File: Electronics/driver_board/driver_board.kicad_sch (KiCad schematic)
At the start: 0 parts

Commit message: [pcb] Added MCU, current sense parts
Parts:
- added J1: Conn_ST_STDC14, Connector_PinHeader_1.27mm:PinHeader_2x07_P1.27mm_Vertical_SMD, symbol Connector:Conn_ST_STDC14
- added R1: 7m, Resistor_SMD:R_2512_6332Metric, symbol Device:R_Small
- added U1: INA241A2xDDF, Package_TO_SOT_SMD:SOT-23-8, symbol Amplifier_Current:INA241A2xDDF
- added U2: STM32G491CCT6, Package_QFP:LQFP-48_7x7mm_P0.5mm, symbol DWlib:STM32G491CCT6
- added U3: REF3433TIDBVR, Package_TO_SOT_SMD:SOT-23-6, symbol DWlib:REF3433TIDBVR
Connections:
- new net: U1.2 (GND), U1.4 (GND)
- new net: J1.5 (GND), J1.7 (GND)
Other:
- company: (none) -> D. Watman

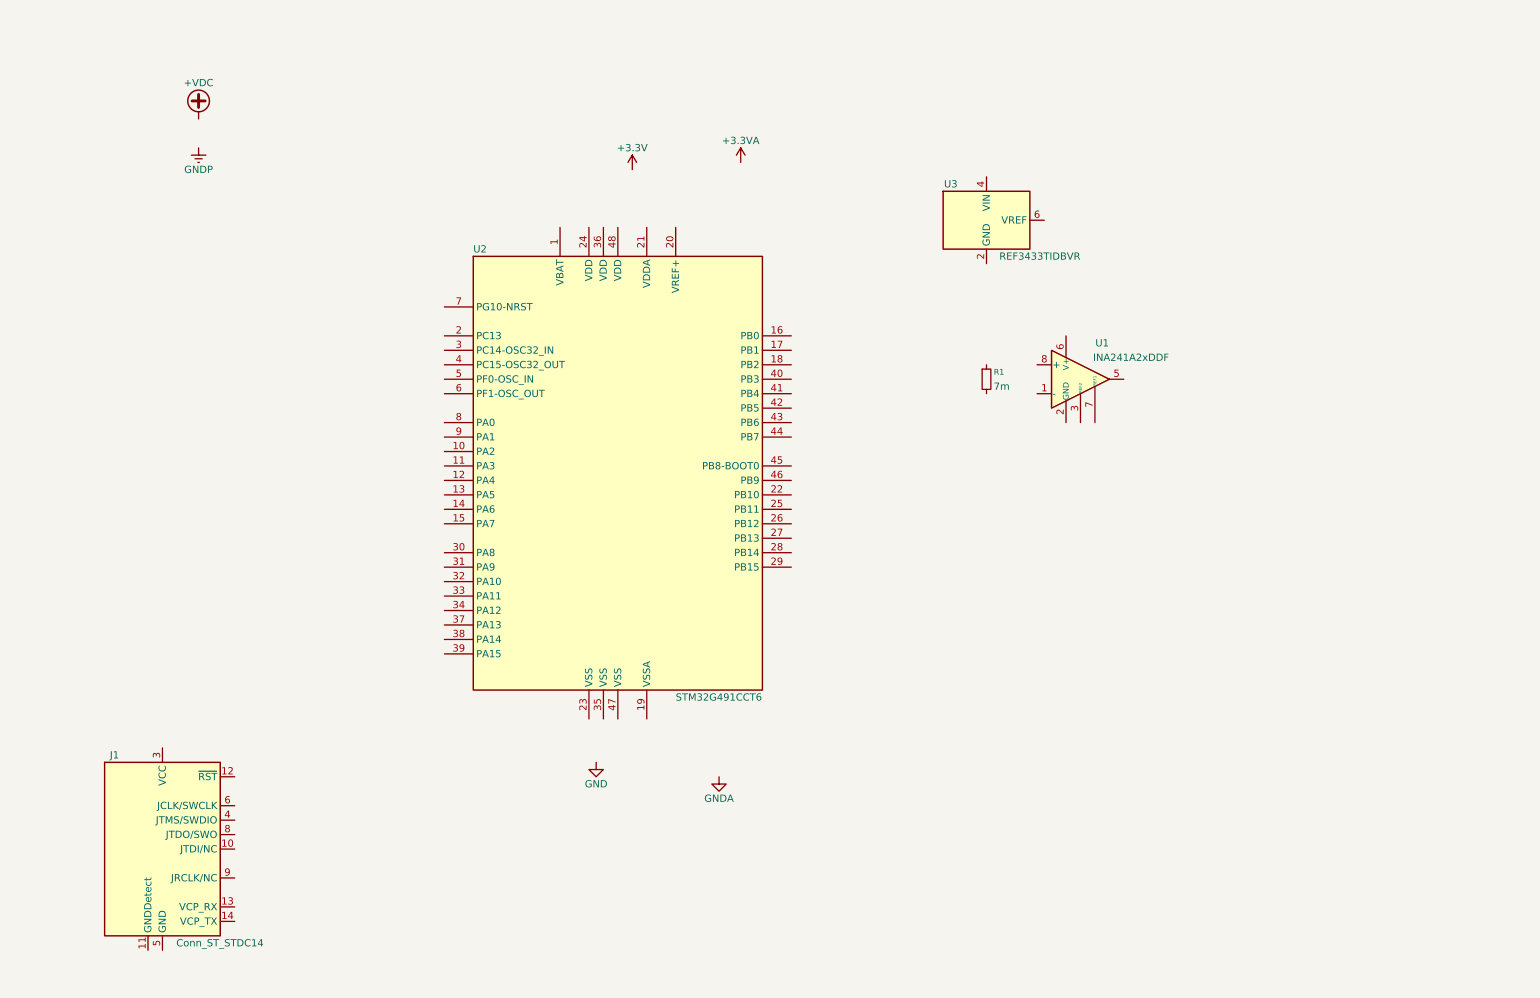
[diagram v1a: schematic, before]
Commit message: Added H-bridge
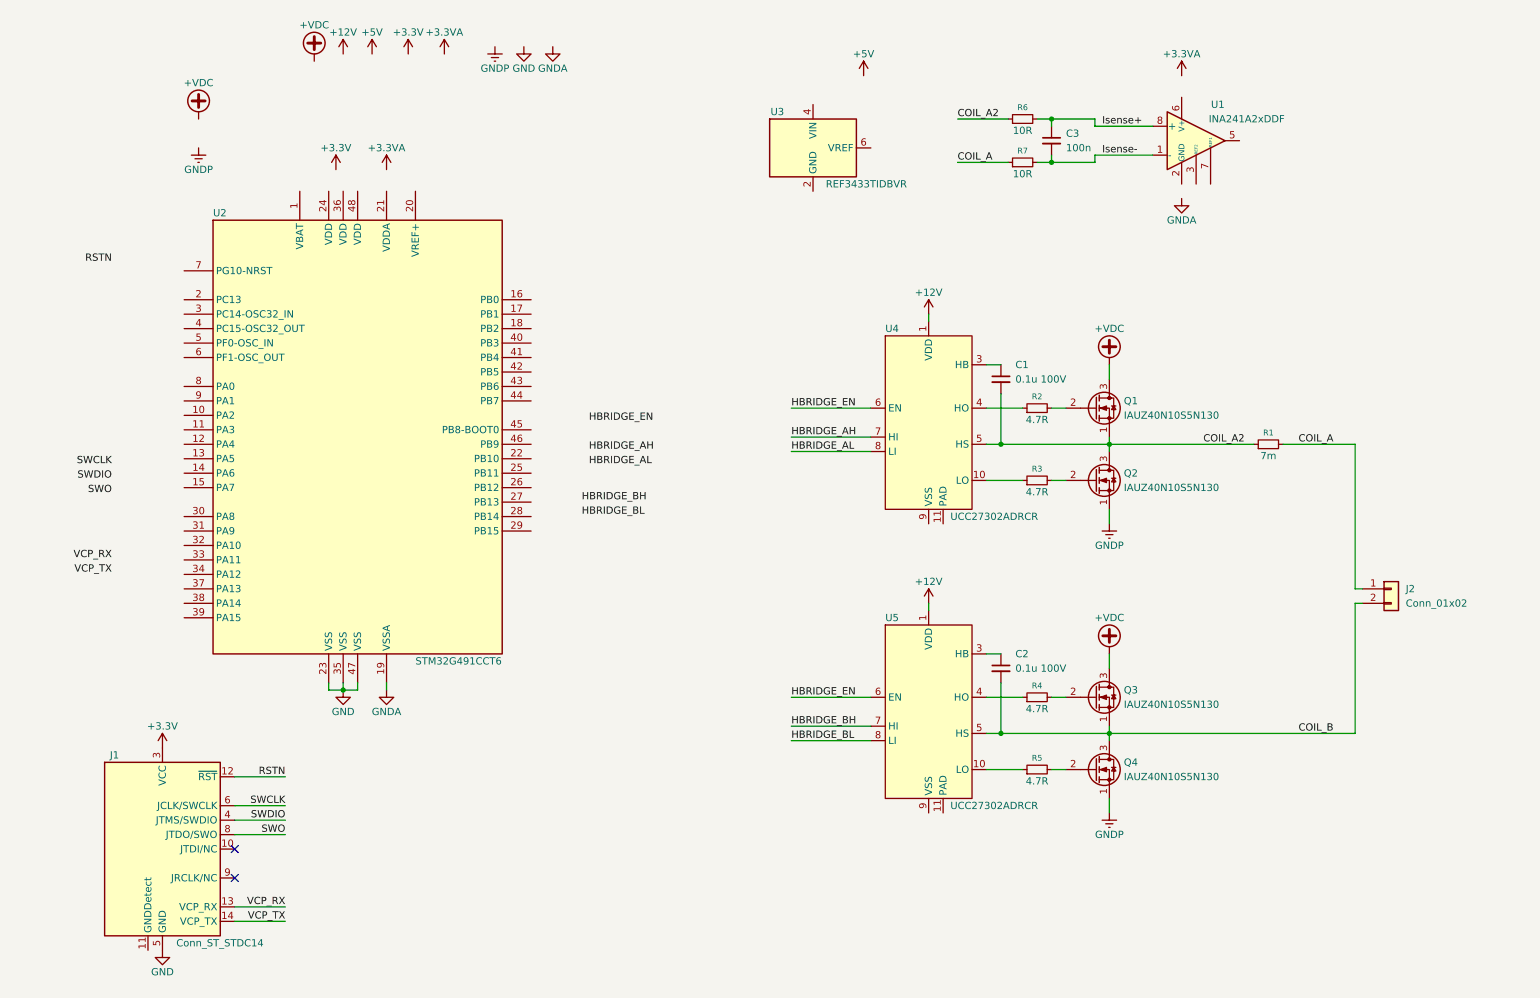
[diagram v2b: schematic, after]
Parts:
- added C1, C2: 0.1u 100V, symbol Device:C_Small
- added C3: 100n, symbol Device:C_Small
- added J2: Conn_01x02, symbol Connector_Generic:Conn_01x02
- added Q1, Q2, Q3, Q4: IAUZ40N10S5N130, DWlib:Infineon_PG-TSDSON-8-33, symbol DWlib:IAUZ40N10S5N130
- added R2, R3, R4, R5: 4.7R, symbol Device:R_Small
- added R6, R7: 10R, symbol Device:R_Small
- added U4, U5: UCC27302ADRCR, DWlib:TI_VSON-10-1EP_3x3mm_P0.5mm_EP1.65x2.4mm, symbol DWlib:UCC27302ADRCR
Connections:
- net +3.3V: now also J1.3 (VCC)
- net +VDC: now also Q1.3 (D), Q3.3 (D)
- net GND: now also J1.5 (GND), J1.7 (GND), U2.23 (VSS), U2.35 (VSS), U2.47 (VSS)
- net GNDA: now also U2.19 (VSSA)
- net GNDP: now also Q2.1 (S), Q4.1 (S)
- net COIL_A2: now reaches R1.1
- net COIL_A2: now also C1.2, Q1.1 (S), Q2.3 (D), R6.1, U4.5 (HS)
- net COIL_A: now reaches R1.2
- net COIL_A: now also J2.1 (Pin_1), R7.1
- net Isense-: now reaches U1.1 (-)
- net Isense-: now also C3.2, R7.2
- net Isense+: now reaches U1.8 (+)
- net Isense+: now also C3.1, R6.2
- net RSTN: now reaches J1.12 (~{RST})
- net VCP_RX: now reaches J1.13 (VCP_RX)
- net VCP_TX: now reaches J1.14 (VCP_TX)
- net SWDIO: now reaches J1.4 (JTMS/SWDIO)
- net SWCLK: now reaches J1.6 (JCLK/SWCLK)
- net SWO: now reaches J1.8 (JTDO/SWO)
- new net: C1.1, U4.3 (HB)
- new net: Q4.2 (G), R5.2
- new net: Q2.2 (G), R3.2
- new net: R4.1, U5.4 (HO)
- new net: Q3.2 (G), R4.2
- new net: R3.1, U4.10 (LO)
- new net: R2.1, U4.4 (HO)
- new net: C2.1, U5.3 (HB)
- new net: Q1.2 (G), R2.2
- new net: R5.1, U5.10 (LO)
- new net +12V: U4.1 (VDD), U5.1 (VDD)
- new net COIL_B: C2.2, J2.2 (Pin_2), Q3.1 (S), Q4.3 (D), U5.5 (HS)
- new net HBRIDGE_AH: U4.7 (HI)
- new net HBRIDGE_AL: U4.8 (LI)
- new net HBRIDGE_BH: U5.7 (HI)
- new net HBRIDGE_BL: U5.8 (LI)
- new net HBRIDGE_EN: U4.6 (EN), U5.6 (EN)
- no-connect marks 0 -> 2
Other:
- moved on the sheet: R1, U1, U2, U3

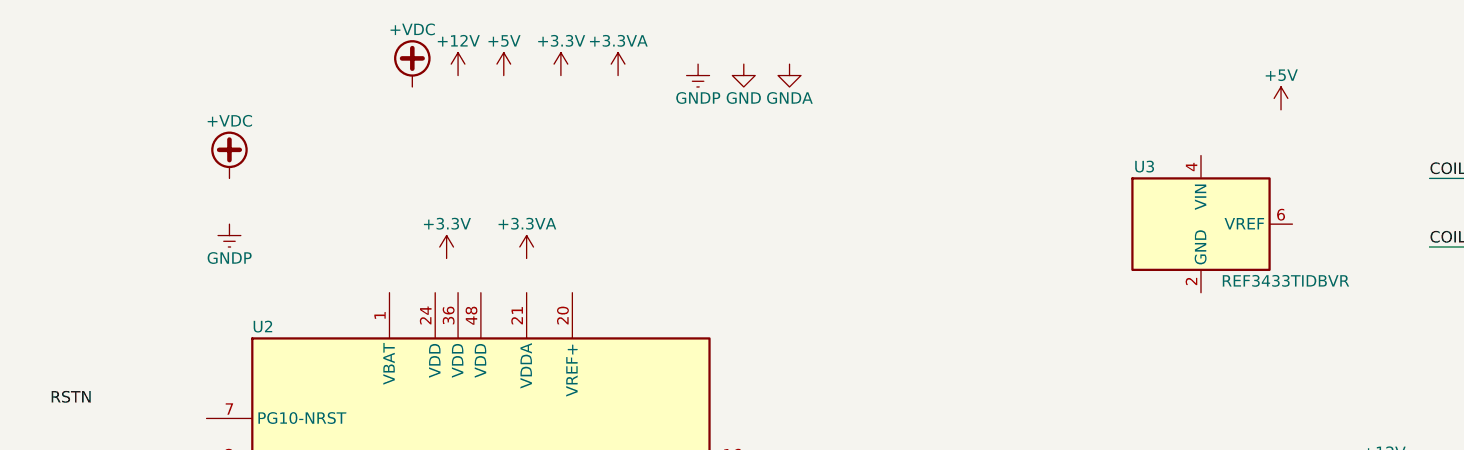
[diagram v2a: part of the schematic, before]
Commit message: [pcb] Added HV DC-DC converter
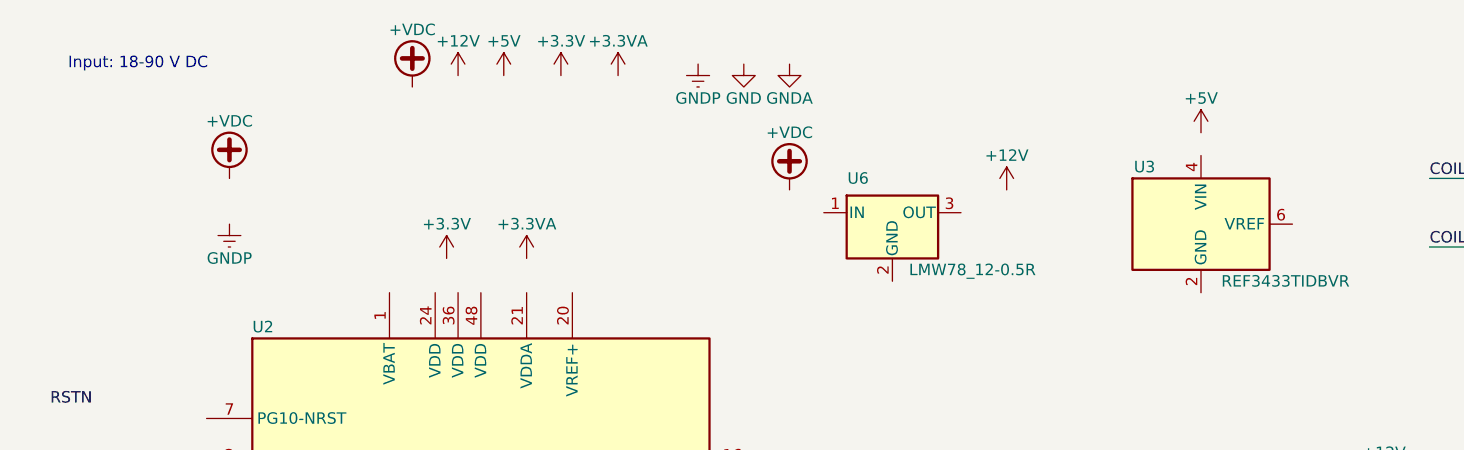
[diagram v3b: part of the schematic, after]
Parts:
- added U6: LMW78_12-0.5R, DWlib:Converter_DCDC_GAPTEC_LMW78_THT, symbol DWlib:LMW78_0.5R
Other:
- note added: "Input: 18-90 V DC"
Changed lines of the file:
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@@
 		(company "D. Watman")
 	)
+	(text "Input: 18-90 V DC"
+		(exclude_from_sim no)
+		(at 39.37 20.32 0)
+		(effects
+			(font
+				(size 1.27 1.27)
+			)
+		)
+	)
 	(junction
 		(at 74.93 133.35)
@@
 	)
 	(symbol
+		(lib_id "DWlib:LMW78_0.5R")
+		(at 123.19 36.83 0)
+		(unit 1)
+		(exclude_from_sim no)
+		(in_bom yes)
+		(on_board yes)
+		(dnp no)
+		(property "Reference" "U6"
+			(at 119.38 33.02 0)
+			(effects
+				(font
+					(size 1.27 1.27)
+				)
+			)
+		)
+		(property "Value" "LMW78_12-0.5R"
+			(at 132.08 43.18 0)
+			(effects
+				(font
+					(size 1.27 1.27)
+				)
+			)
+		)
+		(property "Footprint" "DWlib:Converter_DCDC_GAPTEC_LMW78_THT"
+			(at 124.46 43.18 0)
+			(effects
+				(font
+					(size 1.27 1.27)
+					(italic yes)
+				)
+				(justify left)
+				(hide yes)
+			)
+		)
+		(property "Datasheet" "https://gaptec-electronic.com/datenblaetter/LMW78_0.5R.pdf"
+			(at 123.19 36.83 0)
+			(effects
+				(font
+					(size 1.27 1.27)
+				)
+				(hide yes)
+			)
+		)
+		(property "Description" "0.5A Step-Down DC/DC-Regulator, up to 90V input, non-isolated, -40°C to +85°C, SIP3"
+			(at 123.19 36.83 0)
+			(effects
+				(font
+					(size 1.27 1.27)
+				)
+				(hide yes)
+			)
+		)
+		(property "MPN" "LMW78_12-0.5R"
+			(at 123.19 36.83 0)
+			(effects
+				(font
+					(size 1.27 1.27)
+				)
+				(hide yes)
+			)
+		)
+		(pin "2"
+		)
+		(pin "3"
+		)
+		(pin "1"
+		)
+		(instances
+			(project ""
+				(path "/90d9ae7d-4001-450f-acdb-4ca976b51116"
+					(reference "U6")
+					(unit 1)
+				)
+			)
+		)
+	)
+	(symbol
 		(lib_id "power:GNDA")
 		(at 111.76 20.32 0)
@@
 	(symbol
 		(lib_id "power:+3.3V")
-		(at 166.37 25.4 0)
+		(at 157.48 27.94 0)
 		(unit 1)
 		(exclude_from_sim no)
@@
 		(dnp no)
 		(property "Reference" "#PWR012"
-			(at 166.37 29.21 0)
+			(at 157.48 31.75 0)
 			(effects
 				(font
@@
 		)
 		(property "Value" "+5V"
-			(at 166.37 21.59 0)
+			(at 157.48 24.13 0)
 			(effects
 				(font
@@
 		)
 		(property "Footprint" ""
-			(at 166.37 25.4 0)
+			(at 157.48 27.94 0)
 			(effects
 				(font
@@
 		)
 		(property "Datasheet" ""
-			(at 166.37 25.4 0)
+			(at 157.48 27.94 0)
 			(effects
 				(font
@@
 		)
 		(property "Description" "Power symbol creates a global label with name \"+3.3V\""
-			(at 166.37 25.4 0)
+			(at 157.48 27.94 0)
 			(effects
 				(font
@@
 	)
 	(symbol
+		(lib_id "power:+3.3V")
+		(at 135.89 34.29 0)
+		(unit 1)
+		(exclude_from_sim no)
+		(in_bom yes)
+		(on_board yes)
+		(dnp no)
+		(property "Reference" "#PWR027"
+			(at 135.89 38.1 0)
+			(effects
+				(font
+					(size 1.27 1.27)
+				)
+				(hide yes)
+			)
+		)
+		(property "Value" "+12V"
+			(at 135.89 30.48 0)
+			(effects
+				(font
+					(size 1.27 1.27)
+				)
+			)
+		)
+		(property "Footprint" ""
+			(at 135.89 34.29 0)
+			(effects
+				(font
+					(size 1.27 1.27)
+				)
+				(hide yes)
+			)
+		)
+		(property "Datasheet" ""
+			(at 135.89 34.29 0)
+			(effects
+				(font
+					(size 1.27 1.27)
+				)
+				(hide yes)
+			)
+		)
+		(property "Description" "Power symbol creates a global label with name \"+3.3V\""
+			(at 135.89 34.29 0)
+			(effects
+				(font
+					(size 1.27 1.27)
+				)
+				(hide yes)
+			)
+		)
+		(pin "1"
+		)
+		(instances
+			(project "driver_board"
+				(path "/90d9ae7d-4001-450f-acdb-4ca976b51116"
+					(reference "#PWR027")
+					(unit 1)
+				)
+			)
+		)
+	)
+	(symbol
 		(lib_id "DWlib:UCC27302ADRCR")
 		(at 177.8 137.16 0)
@@
 					(unit 1)
 				)
+			)
+		)
+	)
+	(symbol
+		(lib_id "power:+VDC")
+		(at 111.76 34.29 0)
+		(unit 1)
+		(exclude_from_sim no)
+		(in_bom yes)
+		(on_board yes)
+		(dnp no)
+		(property "Reference" "#PWR026"
+			(at 111.76 36.83 0)
+			(effects
+				(font
+					(size 1.27 1.27)
+				)
+				(hide yes)
+			)
+		)
+		(property "Value" "+VDC"
+			(at 111.76 27.94 0)
+			(effects
+				(font
+					(size 1.27 1.27)
+				)
+			)
+		)
+		(property "Footprint" ""
+			(at 111.76 34.29 0)
+			(effects
+				(font
+					(size 1.27 1.27)
+				)
+				(hide yes)
+			)
+		)
+		(property "Datasheet" ""
+			(at 111.76 34.29 0)
+			(effects
+				(font
+					(size 1.27 1.27)
+				)
+				(hide yes)
+			)
+		)
+		(property "Description" "Power symbol creates a global label with name \"+VDC\""
+			(at 111.76 34.29 0)
+			(effects
+				(font
+					(size 1.27 1.27)
+				)
+				(hide yes)
+			)
+		)
+		(pin "1"
+		)
+		(instances
+			(project "driver_board"
+				(path "/90d9ae7d-4001-450f-acdb-4ca976b51116"
+					(reference "#PWR026")
+					(unit 1)
+				)
